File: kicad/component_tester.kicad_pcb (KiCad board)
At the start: 2 copper layers, 100.4 x 83 mm, 86 parts, among them IC201 MCP1640, IC202 ATmega328P-MMH, IC301 FT232RL, IC302 MAX1811, J301 0R-JUMPA, J302 0R-JUMPA, Q201 8 MHz, Q401 BSS138, Q402 BSS138, SW201 Tactile Switch, T201 PMV65XP, T202 BSS84, T203 BSS123, T204 BC847, T301 BSS123, U401 VREG_SOT23-5, X201 MICRO-USB, X202 ISP

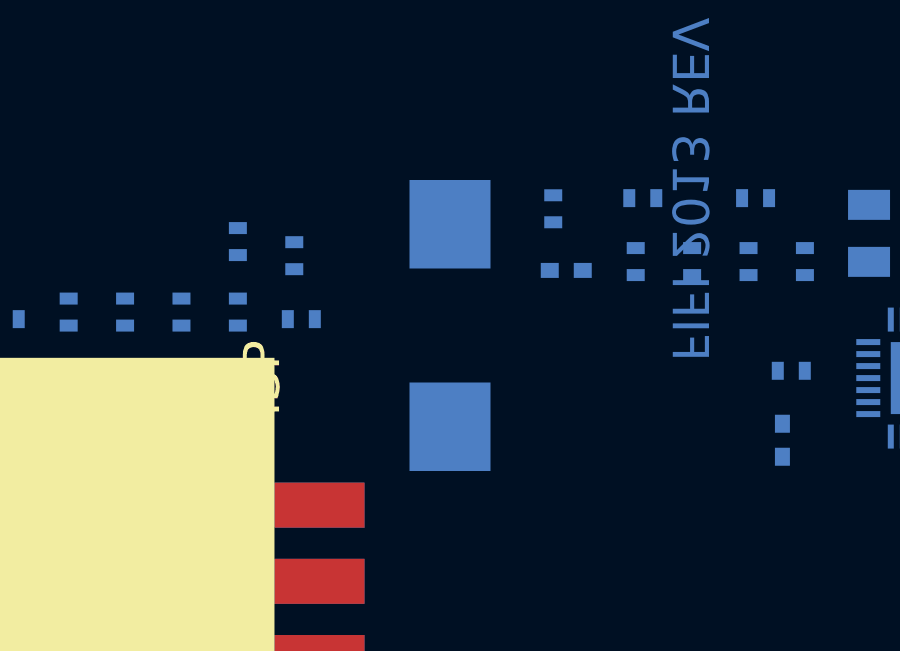
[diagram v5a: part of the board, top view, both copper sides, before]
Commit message: Reduce atmega decoupling cap to 10uF
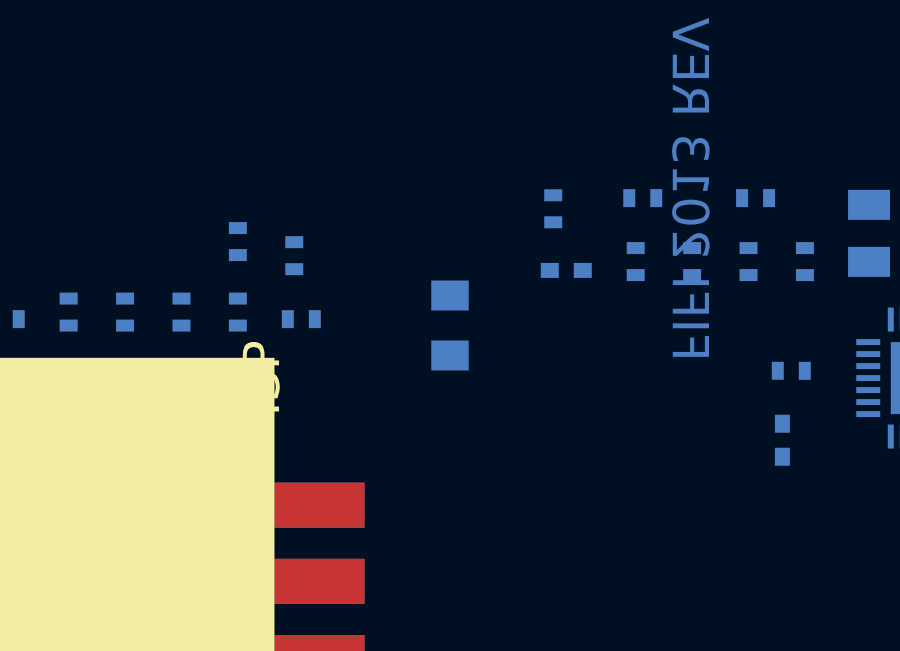
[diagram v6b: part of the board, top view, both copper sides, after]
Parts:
- C201: value 100u -> 10uF; footprint component_tester:D_7343-31W -> KiCad/Capacitors_SMD.pretty:C_0805
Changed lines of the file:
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@@
     (46 B.CrtYd user)
     (47 F.CrtYd user hide)
-    (48 B.Fab user)
+    (48 B.Fab user hide)
     (49 F.Fab user hide)
   )
@@
     (add_net VIN)
   )
+  (module KiCad/Capacitors_SMD.pretty:C_0805 (layer Bottom)
+    (at 105.262581 35.525733 90)
+    (descr "Capacitor SMD 0805, reflow soldering, AVX (see smccp.pdf)")
+    (tags "capacitor 0805")
+    (attr smd)
+    (fp_text reference C201 (at 0 1.5 90) (layer B.SilkS)
+      (effects (font (size 1 1) (thickness 0.15)) (justify mirror))
+    )
+    (fp_text value 10uF (at 0 -1.75 90) (layer B.Fab)
+      (effects (font (size 1 1) (thickness 0.15)) (justify mirror))
+    )
+    (fp_text user %R (at 0 1.5 90) (layer B.Fab)
+      (effects (font (size 1 1) (thickness 0.15)) (justify mirror))
+    )
+    (fp_line (start -1 -0.62) (end -1 0.62) (layer B.Fab) (width 0.1))
+    (fp_line (start 1 -0.62) (end -1 -0.62) (layer B.Fab) (width 0.1))
+    (fp_line (start 1 0.62) (end 1 -0.62) (layer B.Fab) (width 0.1))
+    (fp_line (start -1 0.62) (end 1 0.62) (layer B.Fab) (width 0.1))
+    (fp_line (start 0.5 0.85) (end -0.5 0.85) (layer B.SilkS) (width 0.12))
+    (fp_line (start -0.5 -0.85) (end 0.5 -0.85) (layer B.SilkS) (width 0.12))
+    (fp_line (start -1.75 0.88) (end 1.75 0.88) (layer B.CrtYd) (width 0.05))
+    (fp_line (start -1.75 0.88) (end -1.75 -0.87) (layer B.CrtYd) (width 0.05))
+    (fp_line (start 1.75 -0.87) (end 1.75 0.88) (layer B.CrtYd) (width 0.05))
+    (fp_line (start 1.75 -0.87) (end -1.75 -0.87) (layer B.CrtYd) (width 0.05))
+    (pad 1 smd rect (at -1 0 90) (size 1 1.25) (layers Bottom B.Paste B.Mask))
+    (pad 2 smd rect (at 1 0 90) (size 1 1.25) (layers Bottom B.Paste B.Mask))
+    (model Capacitors_SMD.3dshapes/C_0805.wrl
+      (at (xyz 0 0 0))
+      (scale (xyz 1 1 1))
+      (rotate (xyz 0 0 0))
+    )
+  )
   (module component_tester:TE_1981568-1 (layer Bottom)
     (at 107.36 61.64 270)
@@
       (net 37 "Net-(IC201-Pad3)") (solder_mask_margin 0.0762))
   )
-  (module component_tester:D_7343-31W (layer Bottom)
-    (at 105.262581 35.525733 90)
-    (descr "<b>Chip Capacitor Type KEMET D / EIA 7343-21</b><p>\nKEMET V / EIA 7343-20, KEMET X / EIA 7343-43 Wafe solder")
-    (fp_text reference C201 (at -3.65 2.3 270) (layer B.SilkS)
-      (effects (font (size 1.2065 1.2065) (thickness 0.09652)) (justify right top mirror))
-    )
-    (fp_text value 100u (at -3.65 -3.575 270) (layer B.SilkS)
-      (effects (font (size 1.2065 1.2065) (thickness 0.09652)) (justify right top mirror))
-    )
-    (fp_poly (pts (xy 2.675 -2.125) (xy 3.15 -2.125) (xy 3.15 2.125) (xy 2.675 2.125)) (layer B.Fab) (width 0))
-    (fp_poly (pts (xy 3.5 -1.2) (xy 3.65 -1.2) (xy 3.65 1.2) (xy 3.5 1.2)) (layer B.Fab) (width 0))
-    (fp_poly (pts (xy -3.65 -1.2) (xy -3.5 -1.2) (xy -3.5 1.2) (xy -3.65 1.2)) (layer B.Fab) (width 0))
-    (fp_line (start -3.45 -2.1) (end -3.45 2.1) (layer B.Fab) (width 0.1016))
-    (fp_line (start 3.45 -2.1) (end -3.45 -2.1) (layer B.Fab) (width 0.1016))
-    (fp_line (start 3.45 2.1) (end 3.45 -2.1) (layer B.Fab) (width 0.1016))
-    (fp_line (start -3.45 2.1) (end 3.45 2.1) (layer B.Fab) (width 0.1016))
-    (pad - smd rect (at -3.375 0 90) (size 2.95 2.7) (layers Bottom B.Paste B.Mask)
-      (net 1 GND) (solder_mask_margin 0.0762))
-    (pad + smd rect (at 3.375 0 90) (size 2.95 2.7) (layers Bottom B.Paste B.Mask)
-      (net 8 +5V) (solder_mask_margin 0.0762))
-  )
   (module component_tester:SOT23 (layer Bottom)

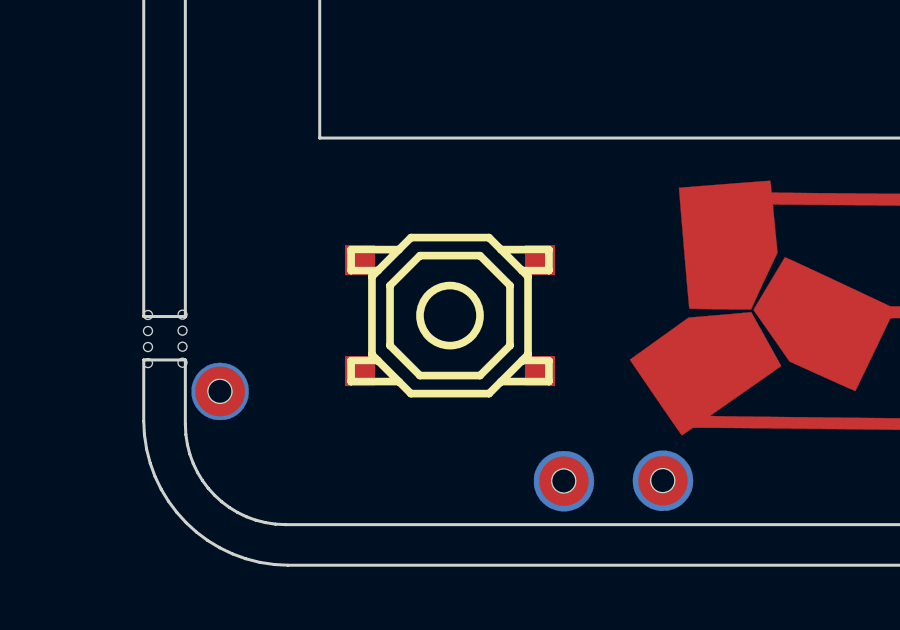
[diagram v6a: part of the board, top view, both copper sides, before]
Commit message: Use panasonic evq for tactile switch
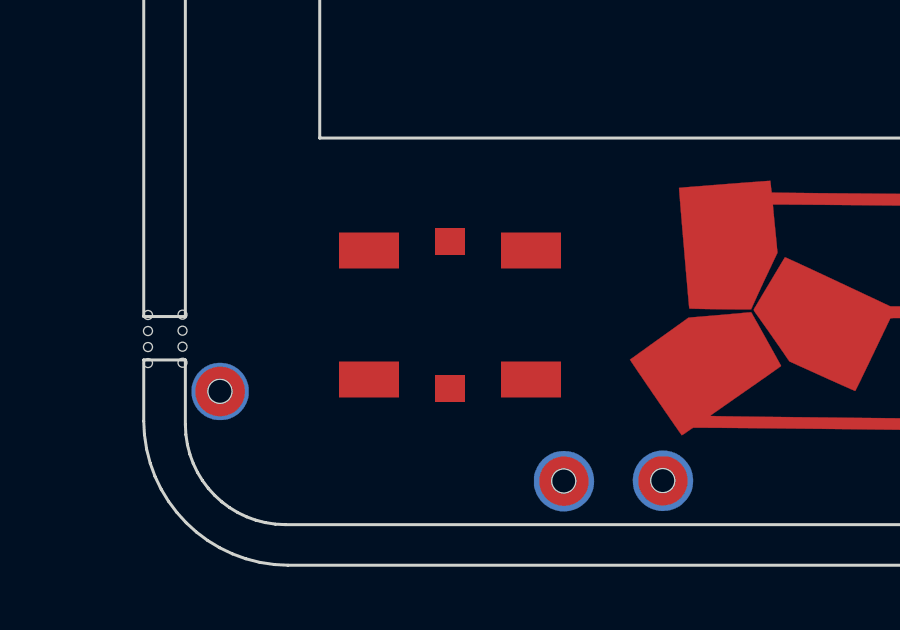
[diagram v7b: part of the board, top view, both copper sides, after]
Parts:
- SW201: value Tactile Switch -> EVQ; footprint smisioto.eu/kicad_libs/modules/w_switch.pretty:smd_push2 -> component_tester:PANASONIC_EVQ
- turned SW201 to 270 degrees
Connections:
- C201 pad 1: (no net) -> +5V
- C201 pad 2: (no net) -> GND
- SW201 pad 1: (no net) -> Net-(C203-Pad1)
- SW201 pad 2: (no net) -> Net-(C203-Pad1)
- SW201 pad 3: (no net) -> Net-(D203-Pad1)
- SW201 pad 4: (no net) -> Net-(D203-Pad1)
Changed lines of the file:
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@@
     (zones 0)
     (modules 86)
-    (nets 95)
+    (nets 97)
   )
   (page A4)
@@
     (46 B.CrtYd user)
     (47 F.CrtYd user hide)
-    (48 B.Fab user hide)
+    (48 B.Fab user)
     (49 F.Fab user hide)
   )
@@
   (net 93 "Net-(OLED1-Pad16)")
   (net 94 "Net-(X201-Pad6)")
+  (net 95 "Net-(SW201-Pad6)")
+  (net 96 "Net-(SW201-Pad5)")
   (net_class Default "This is the default net class."
     (clearance 0.1524)
@@
     (add_net "Net-(R205-Pad1)")
     (add_net "Net-(R213-Pad1)")
+    (add_net "Net-(SW201-Pad5)")
+    (add_net "Net-(SW201-Pad6)")
     (add_net "Net-(U401-Pad4)")
     (add_net "Net-(X201-Pad4)")
@@
     (add_net VIN)
   )
+  (module component_tester:PANASONIC_EVQ (layer Top)
+    (at 160.61 107.7 270)
+    (attr smd)
+    (fp_text reference SW201 (at 0 0 270) (layer F.Fab)
+      (effects (font (size 1.2 1.2) (thickness 0.12)))
+    )
+    (fp_text value EVQ (at 0 0 270) (layer F.Fab)
+      (effects (font (size 1 1) (thickness 0.1)))
+    )
+    (fp_line (start -1.29 -2.51) (end 1.29 -2.51) (layer F.Fab) (width 0.12))
+    (fp_line (start 2.51 -1.44) (end 2.51 -0.76) (layer F.Fab) (width 0.12))
+    (fp_line (start 2.51 0.76) (end 2.51 1.44) (layer F.Fab) (width 0.12))
+    (fp_line (start -1.29 2.51) (end 1.29 2.51) (layer F.Fab) (width 0.12))
+    (fp_line (start -2.51 -1.44) (end -2.51 -0.76) (layer F.Fab) (width 0.12))
+    (fp_line (start -2.51 0.76) (end -2.51 1.44) (layer F.Fab) (width 0.12))
+    (fp_text user REF** (at 0 0 270) (layer F.Fab) hide
+      (effects (font (size 1 1) (thickness 0.1)))
+    )
+    (fp_line (start -2.45 -2.45) (end 2.45 -2.45) (layer F.Fab) (width 0.1))
+    (fp_line (start 2.45 -2.45) (end 2.45 2.45) (layer F.Fab) (width 0.1))
+    (fp_line (start 2.45 2.45) (end -2.45 2.45) (layer F.Fab) (width 0.1))
+    (fp_line (start -2.45 2.45) (end -2.45 -2.45) (layer F.Fab) (width 0.1))
+    (fp_circle (center 0 0) (end 0 0.5) (layer F.CrtYd) (width 0.05))
+    (fp_line (start -0.7 0) (end 0.7 0) (layer F.CrtYd) (width 0.05))
+    (fp_line (start 0 -0.7) (end 0 0.7) (layer F.CrtYd) (width 0.05))
+    (fp_line (start -3.15 -3.95) (end 3.15 -3.95) (layer F.CrtYd) (width 0.05))
+    (fp_line (start 3.15 -3.95) (end 3.15 3.95) (layer F.CrtYd) (width 0.05))
+    (fp_line (start 3.15 3.95) (end -3.15 3.95) (layer F.CrtYd) (width 0.05))
+    (fp_line (start -3.15 3.95) (end -3.15 -3.95) (layer F.CrtYd) (width 0.05))
+    (pad 1 smd rect (at -2.15 -2.7 270) (size 1.2 2) (layers Top F.Paste F.Mask)
+      (net 18 "Net-(C203-Pad1)") (solder_mask_margin 0.05))
+    (pad 2 smd rect (at 2.15 -2.7 270) (size 1.2 2) (layers Top F.Paste F.Mask)
+      (net 18 "Net-(C203-Pad1)") (solder_mask_margin 0.05))
+    (pad 3 smd rect (at -2.15 2.7 270) (size 1.2 2) (layers Top F.Paste F.Mask)
+      (net 17 "Net-(D203-Pad1)") (solder_mask_margin 0.05))
+    (pad 4 smd rect (at 2.15 2.7 270) (size 1.2 2) (layers Top F.Paste F.Mask)
+      (net 17 "Net-(D203-Pad1)") (solder_mask_margin 0.05))
+    (pad 5 smd rect (at 2.45 0 270) (size 0.9 1) (layers Top F.Paste F.Mask)
+      (net 96 "Net-(SW201-Pad5)") (solder_mask_margin 0.05))
+    (pad 6 smd rect (at -2.45 0 270) (size 0.9 1) (layers Top F.Paste F.Mask)
+      (net 95 "Net-(SW201-Pad6)") (solder_mask_margin 0.05))
+    (model PANASONIC_EVQ.wrl
+      (at (xyz 0 0 0))
+      (scale (xyz 0.3937 0.3937 0.3937))
+      (rotate (xyz 0 0 0))
+    )
+  )
   (module KiCad/Capacitors_SMD.pretty:C_0805 (layer Bottom)
     (at 105.262581 35.525733 90)
@@
     (fp_line (start 1.75 -0.87) (end 1.75 0.88) (layer B.CrtYd) (width 0.05))
     (fp_line (start 1.75 -0.87) (end -1.75 -0.87) (layer B.CrtYd) (width 0.05))
-    (pad 1 smd rect (at -1 0 90) (size 1 1.25) (layers Bottom B.Paste B.Mask))
-    (pad 2 smd rect (at 1 0 90) (size 1 1.25) (layers Bottom B.Paste B.Mask))
+    (pad 1 smd rect (at -1 0 90) (size 1 1.25) (layers Bottom B.Paste B.Mask)
+      (net 8 +5V))
+    (pad 2 smd rect (at 1 0 90) (size 1 1.25) (layers Bottom B.Paste B.Mask)
+      (net 1 GND))
     (model Capacitors_SMD.3dshapes/C_0805.wrl
       (at (xyz 0 0 0))
@@
       (net 11 "Net-(C209-Pad1)"))
   )
-  (module smisioto.eu/kicad_libs/modules/w_switch.pretty:smd_push2 (layer Top)
-    (at 160.61 107.72 180)
-    (descr "SMD Pushbutton 2")
-    (autoplace_cost180 10)
-    (fp_text reference SW201 (at 0 -3.59918 180) (layer F.Fab)
-      (effects (font (size 1.143 1.27) (thickness 0.1524)))
-    )
-    (fp_text value "Tactile Switch" (at 0 3.59918 180) (layer F.Fab)
-      (effects (font (size 1.143 1.27) (thickness 0.1524)))
-    )
-    (fp_line (start 2.4003 -1.50114) (end 3.29946 -1.50114) (layer F.SilkS) (width 0.254))
-    (fp_line (start 3.29946 -1.50114) (end 3.29946 -2.19964) (layer F.SilkS) (width 0.254))
-    (fp_line (start 3.29946 -2.19964) (end 1.69926 -2.19964) (layer F.SilkS) (width 0.254))
-    (fp_line (start 1.69926 2.19964) (end 3.29946 2.19964) (layer F.SilkS) (width 0.254))
-    (fp_line (start 3.29946 2.19964) (end 3.29946 1.50114) (layer F.SilkS) (width 0.254))
-    (fp_line (start 3.29946 1.50114) (end 2.4003 1.50114) (layer F.SilkS) (width 0.254))
-    (fp_line (start -3.29946 1.50114) (end -3.29946 2.19964) (layer F.SilkS) (width 0.254))
-    (fp_line (start -3.29946 2.19964) (end -1.69926 2.19964) (layer F.SilkS) (width 0.254))
-    (fp_line (start -3.29946 1.50114) (end -2.4003 1.50114) (layer F.SilkS) (width 0.254))
-    (fp_line (start -1.69926 -2.19964) (end -3.29946 -2.19964) (layer F.SilkS) (width 0.254))
-    (fp_line (start -3.29946 -2.19964) (end -3.29946 -1.50114) (layer F.SilkS) (width 0.254))
-    (fp_line (start -3.29946 -1.50114) (end -2.4003 -1.50114) (layer F.SilkS) (width 0.254))
-    (fp_line (start -1.99898 1.00076) (end -1.00076 1.99898) (layer F.SilkS) (width 0.254))
-    (fp_line (start -1.00076 1.99898) (end 1.00076 1.99898) (layer F.SilkS) (width 0.254))
-    (fp_line (start 1.00076 1.99898) (end 1.99898 1.00076) (layer F.SilkS) (width 0.254))
-    (fp_line (start 1.99898 1.00076) (end 1.99898 -1.00076) (layer F.SilkS) (width 0.254))
-    (fp_line (start 1.99898 -1.00076) (end 1.00076 -1.99898) (layer F.SilkS) (width 0.254))
-    (fp_line (start 1.00076 -1.99898) (end -1.00076 -1.99898) (layer F.SilkS) (width 0.254))
-    (fp_line (start -1.00076 -1.99898) (end -1.99898 -1.00076) (layer F.SilkS) (width 0.254))
-    (fp_line (start -1.99898 -1.00076) (end -1.99898 1.00076) (layer F.SilkS) (width 0.254))
-    (fp_line (start -1.30048 2.60096) (end 1.30048 2.60096) (layer F.SilkS) (width 0.254))
-    (fp_line (start -2.60096 -1.30048) (end -2.60096 1.30048) (layer F.SilkS) (width 0.254))
-    (fp_line (start 1.30048 2.60096) (end 2.60096 1.30048) (layer F.SilkS) (width 0.254))
-    (fp_line (start 2.60096 1.30048) (end 2.60096 -1.30048) (layer F.SilkS) (width 0.254))
-    (fp_line (start 2.60096 -1.30048) (end 1.30048 -2.60096) (layer F.SilkS) (width 0.254))
-    (fp_line (start 1.30048 -2.60096) (end -1.30048 -2.60096) (layer F.SilkS) (width 0.254))
-    (fp_line (start -2.60096 1.30048) (end -1.30048 2.60096) (layer F.SilkS) (width 0.254))
-    (fp_line (start -1.30048 -2.60096) (end -2.60096 -1.30048) (layer F.SilkS) (width 0.254))
-    (fp_circle (center 0 0) (end -1.00076 0) (layer F.SilkS) (width 0.254))
-    (pad 1 smd rect (at -2.99974 -1.84912 180) (size 1.00076 1.00076) (layers Top F.Paste F.Mask))
-    (pad 2 smd rect (at 2.99974 1.84912 180) (size 1.00076 1.00076) (layers Top F.Paste F.Mask))
-    (pad 3 smd rect (at -2.99974 1.84912 180) (size 1.00076 1.00076) (layers Top F.Paste F.Mask))
-    (pad 4 smd rect (at 2.99974 -1.84912 180) (size 1.00076 1.00076) (layers Top F.Paste F.Mask))
-    (model walter/switch/smd_push2.wrl
-      (at (xyz 0 0 0))
-      (scale (xyz 1 1 1))
-      (rotate (xyz 0 0 0))
-    )
-  )
   (module KiCad/Crystals.pretty:Crystal_SMD_Abracon_ABM3-2pin_5.0x3.2mm (layer Bottom)

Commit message: Work on placement
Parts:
- moved IC202 89.5 mm to (175.8, 108.1)
- moved C205 87.3 mm to (168.2, 109.6)
- moved Q201 84.3 mm to (170.9, 108.1)
- moved C204 68.7 mm to (168.3, 106.6), turned to 90 degrees
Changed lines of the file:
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@@
     (46 B.CrtYd user)
     (47 F.CrtYd user hide)
-    (48 B.Fab user)
+    (48 B.Fab user hide)
     (49 F.Fab user hide)
   )
@@
     (pad_to_mask_clearance 0.2)
     (aux_axis_origin 0 0)
-    (visible_elements FFFFF77F)
+    (visible_elements FFFFFF7F)
     (pcbplotparams
       (layerselection 0x010fc_ffffffff)
@@
   )
   (module KiCad/Crystals.pretty:Crystal_SMD_Abracon_ABM3-2pin_5.0x3.2mm (layer Bottom)
-    (at 126.405616 36.578294 90)
+    (at 170.92 108.11 90)
     (descr "Abracon Miniature Ceramic Smd Crystal ABM3 http://www.abracon.com/Resonators/abm3.pdf, 5.0x3.2mm^2 package")
     (tags "SMD SMT crystal")
     (attr smd)
-    (fp_text reference Q201 (at 0 -2.794 90) (layer B.SilkS)
+    (fp_text reference Q201 (at 4.05 -0.07 180) (layer B.SilkS)
       (effects (font (size 1 1) (thickness 0.15)) (justify mirror))
     )
@@
   )
   (module KiCad/Capacitors_SMD.pretty:C_0402 (layer Bottom)
-    (at 116.343623 39.350732 270)
+    (at 168.22 109.56 270)
     (descr "Capacitor SMD 0402, reflow soldering, AVX (see smccp.pdf)")
     (tags "capacitor 0402")
@@
   )
   (module KiCad/Capacitors_SMD.pretty:C_0402 (layer Bottom)
-    (at 129.934686 49.580391 270)
+    (at 168.29 106.56 90)
     (descr "Capacitor SMD 0402, reflow soldering, AVX (see smccp.pdf)")
     (tags "capacitor 0402")
     (attr smd)
-    (fp_text reference C204 (at 0 1.27 270) (layer B.SilkS)
+    (fp_text reference C204 (at 1.2 -1.41 90) (layer B.SilkS)
       (effects (font (size 1 1) (thickness 0.15)) (justify mirror))
     )
-    (fp_text value 22p (at 0 -1.27 270) (layer B.Fab)
+    (fp_text value 22p (at 0 -1.27 90) (layer B.Fab)
       (effects (font (size 1 1) (thickness 0.15)) (justify mirror))
     )
-    (fp_text user %R (at 0 1.27 270) (layer B.Fab)
+    (fp_text user %R (at 0 1.27 90) (layer B.Fab)
       (effects (font (size 1 1) (thickness 0.15)) (justify mirror))
     )
@@
     (fp_line (start 1 -0.4) (end 1 0.4) (layer B.CrtYd) (width 0.05))
     (fp_line (start 1 -0.4) (end -1 -0.4) (layer B.CrtYd) (width 0.05))
-    (pad 1 smd rect (at -0.55 0 270) (size 0.6 0.5) (layers Bottom B.Paste B.Mask)
+    (pad 1 smd rect (at -0.55 0 90) (size 0.6 0.5) (layers Bottom B.Paste B.Mask)
       (net 1 GND))
-    (pad 2 smd rect (at 0.55 0 270) (size 0.6 0.5) (layers Bottom B.Paste B.Mask)
+    (pad 2 smd rect (at 0.55 0 90) (size 0.6 0.5) (layers Bottom B.Paste B.Mask)
       (net 48 "Net-(C204-Pad2)"))
     (model Capacitors_SMD.3dshapes/C_0402.wrl
@@
   )
   (module KiCad/Housings_DFN_QFN.pretty:QFN-28-1EP_4x4mm_Pitch0.4mm (layer Bottom)
-    (at 121.155614 37.278294)
+    (at 175.85 108.1)
     (descr "28-Lead Plastic Quad Flat, No Lead Package (MK) - 4x4x0.9 mm Body [QFN]; (see Microchip Packaging Specification 00000049BS.pdf)")
     (tags "QFN 0.4")
